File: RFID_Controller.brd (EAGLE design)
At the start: 77 x 67 mm, 41 parts, among them IC2 MCP23017SP, K1 FTR-K1C, T1 BC547, T2 BC547

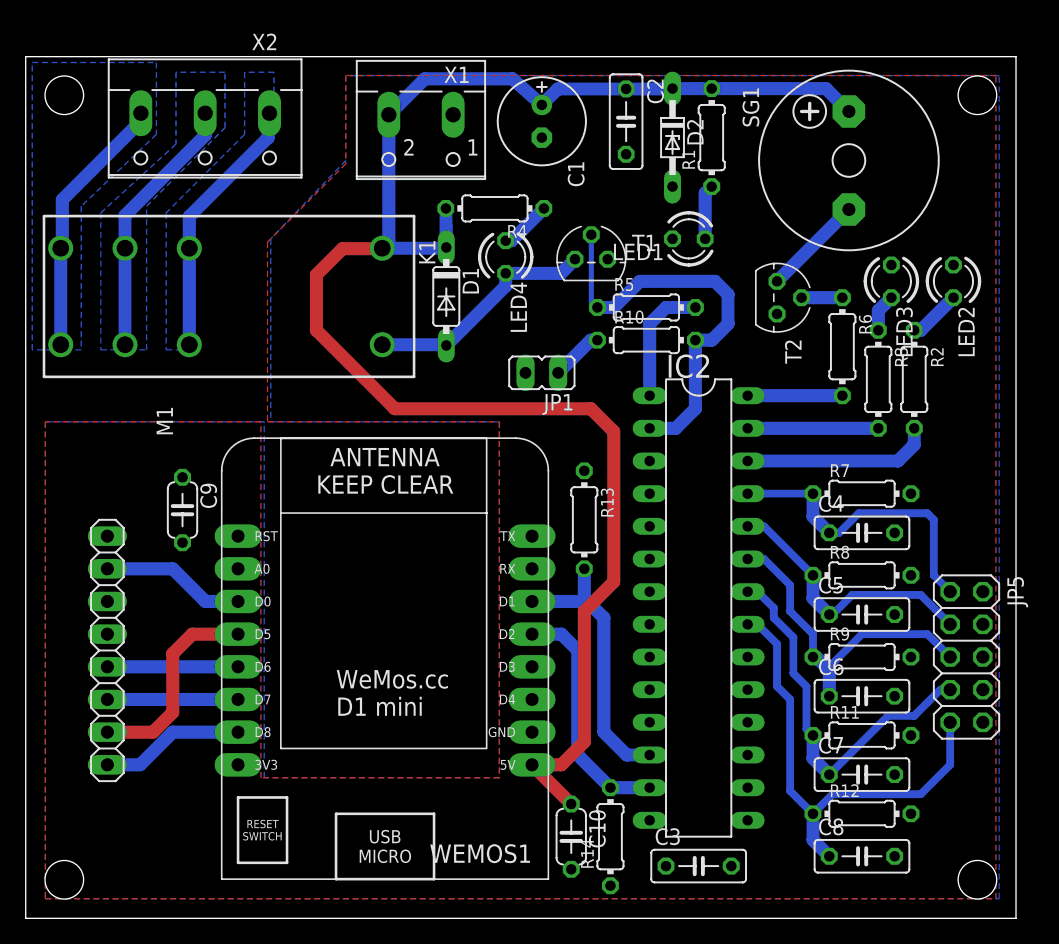
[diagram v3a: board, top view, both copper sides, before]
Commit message: -mod: more distance between drill and HV (upper left corner) -mod: TVS diode instead of Z-Diode -fix: additional resistor to SW Output pin to avoid short circuits. SW input pin measures now full voltage, not only Ube
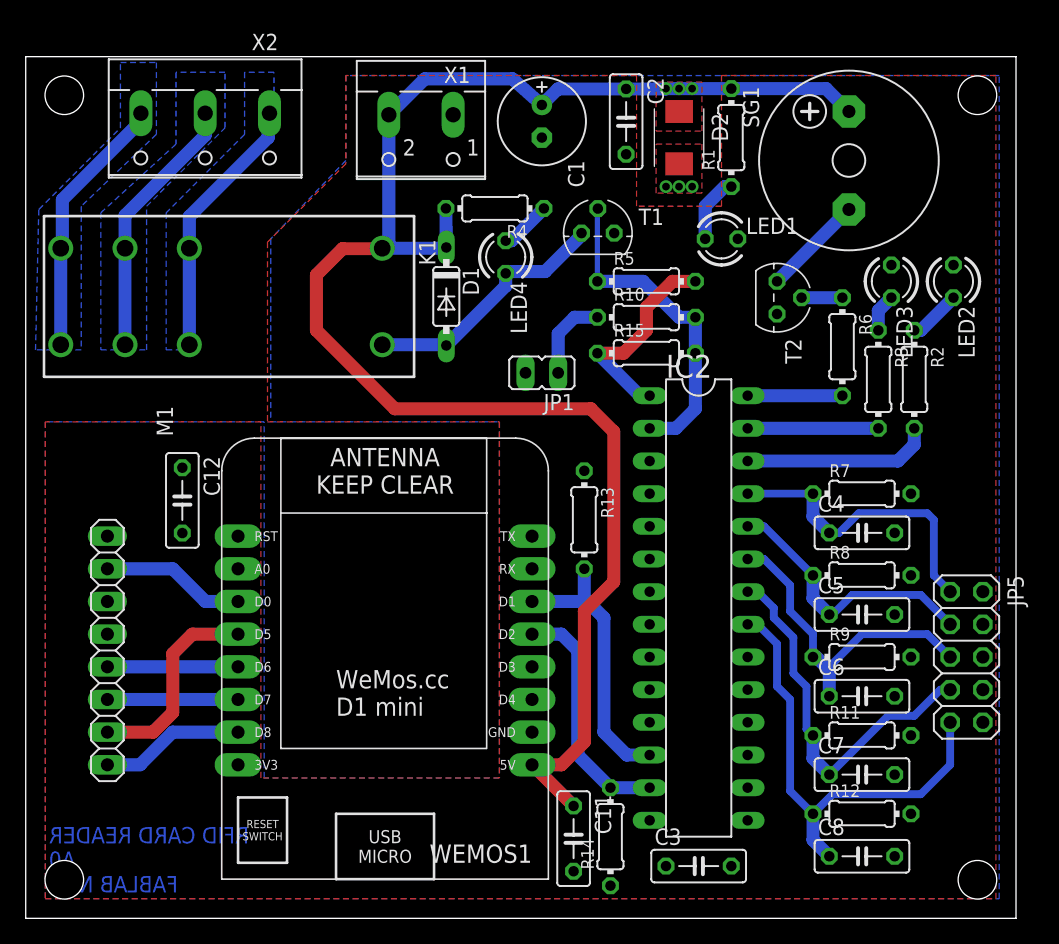
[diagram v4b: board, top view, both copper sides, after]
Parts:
- removed C10, C9: 100p, rcl:C050-024X044
- added C11, C12: 100n, rcl:C050-025X075
- added R15: 1k, rcl:0204/7
- D2: value 5.1V -> SM6T5A; device diode:DO34Z7 -> diode:SMBJ
- moved LED1 2.54 mm to (54.1, 52.8), turned to 0 degrees
- moved T1 2.09 mm to (44.5, 53.3)
- moved R5 2.03 mm to (48.3, 49.5)
- moved R10 1.78 mm to (48.3, 46.7)
- moved R1 1.52 mm to (54.9, 60.7)
- moved D2 0.51 mm to (50.8, 60.7)
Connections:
- removed net VCC: C9.1
- net 3V3: now also C12.1
- net 5V: now also C11.1; no longer C10.1
- net GND: now also C11.2, C12.2; no longer C10.2, C9.2
- net N$8: now also R15.1
- net SW: now also R15.2
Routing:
- net SW: track 32.9 -> 25.7 mm
- net N$8: track 9.67 -> 16.4 mm
- net N$12: track 4.10 -> 6.62 mm
- net N$5: track 18.4 -> 19.8 mm
- net N$1: track 4.27 -> 5.20 mm
- net 5V: track 128.5 -> 128.7 mm, vias 0 -> 3
- added copper zone on layer 1, net 5V
- added copper zone on layer 1, net GND
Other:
- board text added: "RFID CARD READER A0 FABLAB NBG"

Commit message: -mod: Board layout and Schematic in ELAB optimized
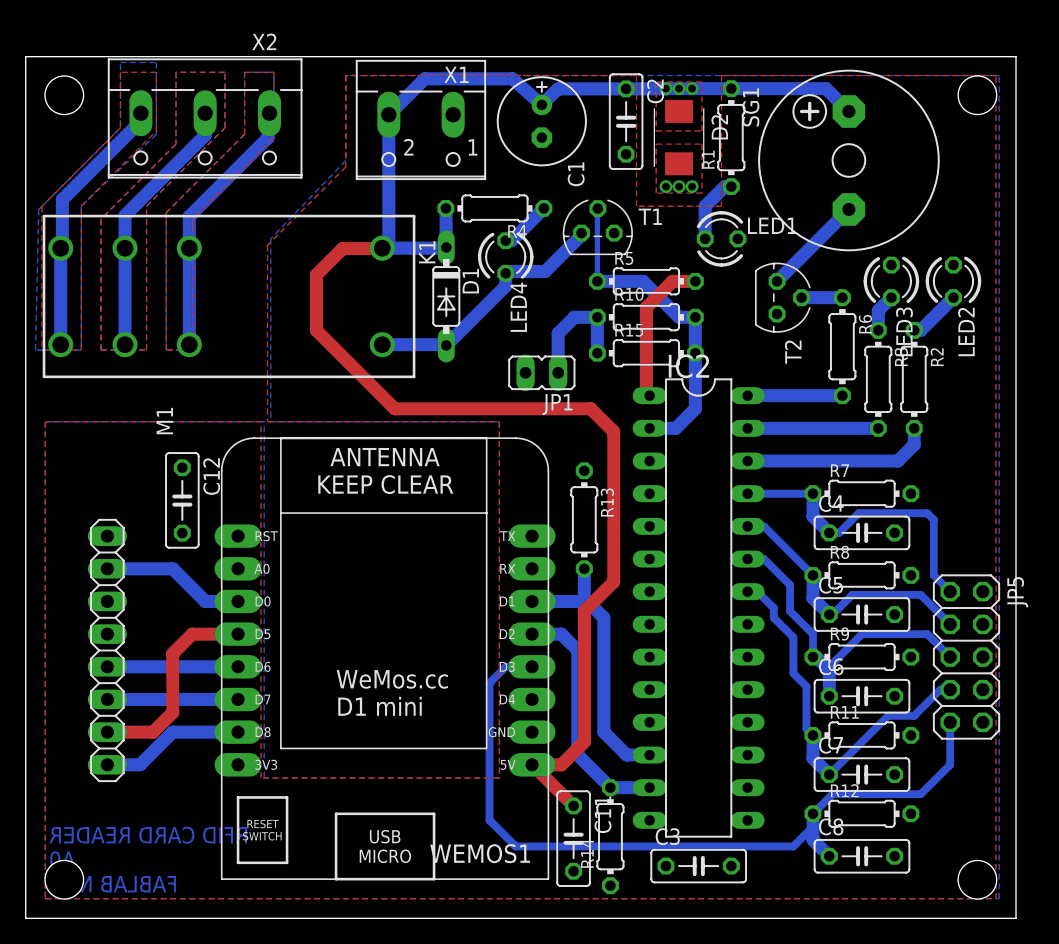
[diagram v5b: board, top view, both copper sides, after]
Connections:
- removed net N$12: JP1.1, R10.1
- new net SW_IN: JP1.1, R10.1, R15.1
- net EX3: now also WEMOS1.D3; no longer IC2.21
- net N$8: no longer R15.1
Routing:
- net EX3: track 36.7 -> 61.5 mm
- net SW_IN: track 0.00 -> 9.42 mm
- net N$12: track 6.62 -> 0.00 mm
- net N$8: track 16.4 -> 12.4 mm
- added copper zone on layer 1, net REL_COMM
- added copper zone on layer 1, net REL_NC
- added copper zone on layer 1, net REL_NO
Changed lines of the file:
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@@
 <polygon width="0.4064" layer="1">
 <vertex x="24.892" y="65.532"/>
-<vertex x="24.892" y="58.674"/>
-<vertex x="18.796" y="52.578"/>
+<vertex x="24.892" y="58.42"/>
+<vertex x="18.796" y="52.324"/>
 <vertex x="18.796" y="38.608"/>
 <vertex x="36.83" y="38.608"/>
@@
 <vertex x="11.684" y="65.786"/>
 <vertex x="11.684" y="60.198"/>
-<vertex x="5.842" y="54.864"/>
+<vertex x="5.842" y="54.356"/>
+<vertex x="5.842" y="44.196"/>
+<vertex x="9.398" y="44.196"/>
+<vertex x="9.398" y="55.372"/>
+<vertex x="15.494" y="61.468"/>
+<vertex x="15.494" y="65.786"/>
+</polygon>
+<polygon width="0.4064" layer="1">
+<vertex x="11.684" y="65.786"/>
+<vertex x="11.684" y="60.198"/>
+<vertex x="5.842" y="54.356"/>
 <vertex x="5.842" y="44.196"/>
 <vertex x="9.398" y="44.196"/>
@@
 <vertex x="7.366" y="66.548"/>
 </polygon>
+<polygon width="0.4064" layer="1">
+<vertex x="10.16" y="65.786"/>
+<vertex x="7.366" y="65.786"/>
+<vertex x="7.366" y="61.468"/>
+<vertex x="1.27" y="55.372"/>
+<vertex x="1.27" y="44.196"/>
+<vertex x="4.318" y="44.196"/>
+<vertex x="4.318" y="55.372"/>
+<vertex x="10.16" y="61.214"/>
+</polygon>
 </signal>
 <signal name="REL_NC" class="1">
@@
 <vertex x="10.922" y="54.864"/>
 </polygon>
+<polygon width="0.4064" layer="1">
+<vertex x="17.018" y="65.786"/>
+<vertex x="19.304" y="65.786"/>
+<vertex x="19.304" y="60.706"/>
+<vertex x="12.954" y="54.356"/>
+<vertex x="12.954" y="53.848"/>
+<vertex x="12.954" y="44.196"/>
+<vertex x="10.922" y="44.196"/>
+<vertex x="10.922" y="54.864"/>
+<vertex x="17.018" y="60.96"/>
+</polygon>
 </signal>
 <signal name="SCL">
@@
 <wire x1="65.024" y1="22.098" x2="70.104" y2="22.098" width="0.6096" layer="16"/>
 <wire x1="70.104" y1="22.098" x2="71.882" y2="20.32" width="0.6096" layer="16"/>
-</signal>
-<signal name="N$12">
-<contactref element="JP1" pad="1"/>
-<contactref element="R10" pad="1"/>
-<wire x1="44.45" y1="46.736" x2="42.672" y2="46.736" width="1.016" layer="16"/>
-<wire x1="42.672" y1="46.736" x2="41.402" y2="45.466" width="1.016" layer="16"/>
-<wire x1="41.402" y1="45.466" x2="41.402" y2="42.418" width="1.016" layer="16"/>
 </signal>
 <signal name="N$2">
@@
 <contactref element="C8" pad="1"/>
 <contactref element="R12" pad="1"/>
-<contactref element="IC2" pad="21"/>
 <contactref element="JP5" pad="9"/>
-<wire x1="56.134" y1="22.86" x2="56.896" y2="22.86" width="0.6096" layer="16"/>
-<wire x1="56.896" y1="22.86" x2="58.42" y2="21.336" width="0.6096" layer="16"/>
-<wire x1="58.42" y1="21.336" x2="58.42" y2="18.034" width="0.6096" layer="16"/>
-<wire x1="58.42" y1="18.034" x2="59.436" y2="17.018" width="0.6096" layer="16"/>
-<wire x1="59.436" y1="17.018" x2="59.436" y2="9.906" width="0.6096" layer="16"/>
-<wire x1="59.436" y1="9.906" x2="61.214" y2="8.128" width="0.6096" layer="16"/>
 <wire x1="61.214" y1="8.128" x2="61.214" y2="6.096" width="1.016" layer="16"/>
 <wire x1="61.214" y1="6.096" x2="62.484" y2="4.826" width="1.016" layer="16"/>
@@
 <wire x1="71.882" y1="11.938" x2="69.596" y2="9.652" width="0.6096" layer="16"/>
 <wire x1="69.596" y1="9.652" x2="62.738" y2="9.652" width="0.6096" layer="16"/>
+<contactref element="WEMOS1" pad="D3"/>
+<wire x1="61.214" y1="8.128" x2="61.214" y2="7.112" width="0.6096" layer="16"/>
+<wire x1="61.214" y1="7.112" x2="59.69" y2="5.588" width="0.6096" layer="16"/>
+<wire x1="59.69" y1="5.588" x2="38.1" y2="5.588" width="0.6096" layer="16"/>
+<wire x1="38.1" y1="5.588" x2="36.068" y2="7.62" width="0.6096" layer="16"/>
+<wire x1="36.068" y1="7.62" x2="36.068" y2="18.288" width="0.6096" layer="16"/>
+<wire x1="36.068" y1="18.288" x2="37.338" y2="19.558" width="0.6096" layer="16"/>
+<wire x1="37.338" y1="19.558" x2="39.37" y2="19.558" width="0.6096" layer="16"/>
 </signal>
 <signal name="N$8">
 <contactref element="R5" pad="2"/>
 <contactref element="IC2" pad="1"/>
-<contactref element="R15" pad="1"/>
 <wire x1="48.514" y1="40.64" x2="47.752" y2="40.64" width="1.016" layer="16"/>
-<wire x1="47.752" y1="40.64" x2="44.45" y2="43.942" width="1.016" layer="16"/>
 <wire x1="52.07" y1="49.53" x2="50.292" y2="49.53" width="1.016" layer="1"/>
 <wire x1="50.292" y1="49.53" x2="48.26" y2="47.498" width="1.016" layer="1"/>
-<wire x1="48.26" y1="47.498" x2="48.26" y2="45.72" width="1.016" layer="1"/>
-<wire x1="48.26" y1="45.72" x2="46.482" y2="43.942" width="1.016" layer="1"/>
-<wire x1="46.482" y1="43.942" x2="44.45" y2="43.942" width="1.016" layer="1"/>
+<wire x1="48.26" y1="47.498" x2="48.26" y2="40.894" width="1.016" layer="1"/>
+<wire x1="48.26" y1="40.894" x2="48.514" y2="40.64" width="1.016" layer="1"/>
+</signal>
+<signal name="SW_IN">
+<contactref element="R15" pad="1"/>
+<contactref element="JP1" pad="1"/>
+<contactref element="R10" pad="1"/>
+<wire x1="44.45" y1="46.736" x2="42.672" y2="46.736" width="1.016" layer="16"/>
+<wire x1="42.672" y1="46.736" x2="41.402" y2="45.466" width="1.016" layer="16"/>
+<wire x1="41.402" y1="45.466" x2="41.402" y2="42.418" width="1.016" layer="16"/>
+<wire x1="44.45" y1="46.736" x2="44.45" y2="43.942" width="1.016" layer="16"/>
 </signal>
 </signals>
